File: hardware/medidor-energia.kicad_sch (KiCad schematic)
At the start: 43 parts, among them J1 Bornera 5 V, J2 Jack 3,5 mm de panel (pinza S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, J3 Jack 3,5 mm de panel (pinza S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, J4 Bornera red L/N, J5 Bornera ZMPT, J6 OLED (GND VCC SCL SDA), J7 Reserva ADC1, SW1 Pulsador de panel 12 mm NA, SW2 Pulsador de panel 12 mm NA, U1 ESP32-DevKitC V4 (38 pines), U2 Módulo ZMPT101B

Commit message: PCB de una cara para fabricar por tóner y gabinete ajustado a ella
- herramientas/generar_pcb.py: PCB de 150 × 90 mm con cobre solo abajo, ruteada con
  Freerouting (4 puentes de alambre), relleno de GND y agujeros M3; DRC sin conexiones
  pendientes ni diferencias con el esquemático
- herramientas/exportar_fabricacion.sh: PDF 1:1 para tóner, Gerber, taladros, guía de
  montaje, lista de puentes, vistas 3D y STEP
- freecad: cables hasta los pads reales (conectores.json), jacks y USB alineados con la PCB,
  tornillos M3, rótulos con tildes y vistas del medidor en Blender
- Documento: sección 7.7 (PCB y alternativa en placa perforada), materiales, cronograma,
  dificultades y anexo; diagrama de bloques con HTTP y la plataforma web
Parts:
- C1: footprint Capacitor_THT:CP_Radial_D8.0mm_P5.00mm -> Capacitor_THT:CP_Radial_D8.0mm_P3.50mm
- C10, C11: footprint Capacitor_THT:C_Disc_D5.0mm_W2.5mm_P2.50mm -> Capacitor_THT:C_Disc_D5.0mm_W2.5mm_P5.00mm
- C9: footprint Capacitor_THT:C_Disc_D7.5mm_W5.0mm_P7.50mm -> Capacitor_THT:C_Disc_D7.5mm_W5.0mm_P5.00mm
- D2, D3, D5: footprint Diode_THT:D_DO-35_SOD27_P5.08mm_Vertical_AnodeUp -> Diode_THT:D_DO-35_SOD27_P7.62mm_Horizontal
- R4: footprint Resistor_THT:R_Axial_DIN0207_L6.3mm_D2.5mm_P5.08mm_Vertical -> Resistor_THT:R_Axial_DIN0207_L6.3mm_D2.5mm_P10.16mm_Horizontal
- R8: footprint Resistor_THT:R_Axial_DIN0207_L6.3mm_D2.5mm_P7.62mm_Horizontal -> Resistor_THT:R_Axial_DIN0207_L6.3mm_D2.5mm_P10.16mm_Horizontal
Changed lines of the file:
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@@
 			)
 		)
-		(property "Footprint" "Capacitor_THT:CP_Radial_D8.0mm_P5.00mm"
+		(property "Footprint" "Capacitor_THT:CP_Radial_D8.0mm_P3.50mm"
 			(at 74.93 55.88 0)
 			(effects
@@
 			)
 		)
-		(property "Footprint" "Diode_THT:D_DO-35_SOD27_P5.08mm_Vertical_AnodeUp"
+		(property "Footprint" "Diode_THT:D_DO-35_SOD27_P7.62mm_Horizontal"
 			(at 96.52 104.14 0)
 			(effects
@@
 			)
 		)
-		(property "Footprint" "Diode_THT:D_DO-35_SOD27_P5.08mm_Vertical_AnodeUp"
+		(property "Footprint" "Diode_THT:D_DO-35_SOD27_P7.62mm_Horizontal"
 			(at 96.52 111.76 0)
 			(effects
@@
 			)
 		)
-		(property "Footprint" "Diode_THT:D_DO-35_SOD27_P5.08mm_Vertical_AnodeUp"
+		(property "Footprint" "Diode_THT:D_DO-35_SOD27_P7.62mm_Horizontal"
 			(at 96.52 157.48 0)
 			(effects
@@
 			)
 		)
-		(property "Footprint" "Resistor_THT:R_Axial_DIN0207_L6.3mm_D2.5mm_P5.08mm_Vertical"
+		(property "Footprint" "Resistor_THT:R_Axial_DIN0207_L6.3mm_D2.5mm_P10.16mm_Horizontal"
 			(at 149.86 111.76 0)
 			(effects
@@
 			)
 		)
-		(property "Footprint" "Resistor_THT:R_Axial_DIN0207_L6.3mm_D2.5mm_P7.62mm_Horizontal"
+		(property "Footprint" "Resistor_THT:R_Axial_DIN0207_L6.3mm_D2.5mm_P10.16mm_Horizontal"
 			(at 160.02 217.17 0)
 			(effects
@@
 			)
 		)
-		(property "Footprint" "Capacitor_THT:C_Disc_D7.5mm_W5.0mm_P7.50mm"
+		(property "Footprint" "Capacitor_THT:C_Disc_D7.5mm_W5.0mm_P5.00mm"
 			(at 172.72 217.17 0)
 			(effects
@@
 			)
 		)
-		(property "Footprint" "Capacitor_THT:C_Disc_D5.0mm_W2.5mm_P2.50mm"
+		(property "Footprint" "Capacitor_THT:C_Disc_D5.0mm_W2.5mm_P5.00mm"
 			(at 317.5 161.29 0)
 			(effects
@@
 			)
 		)
-		(property "Footprint" "Capacitor_THT:C_Disc_D5.0mm_W2.5mm_P2.50mm"
+		(property "Footprint" "Capacitor_THT:C_Disc_D5.0mm_W2.5mm_P5.00mm"
 			(at 317.5 189.23 0)
 			(effects

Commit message: Plataforma sobre Supabase, esquemáticos sin datos personales y redacción revisada
- plataforma: Postgres en Supabase con postgres.js (DATABASE_URL) en lugar de SQLite;
  migración en supabase/migrations con RLS activo; ingesta por lotes en una transacción;
  pnpm db:migrar y .env.ejemplo; pruebas del servicio contra un Postgres de pruebas
- Esquemáticos, PCB y figuras sin nombres ni referencias a asignaturas (revisión B)
- Redacción del documento revisada para un tono más directo y sin exagerar el avance
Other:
- company: Universidad de la Costa (CUC) — Sistemas Embebidos 1 -> (none)
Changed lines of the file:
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@@
 	(title_block
 		(title "Medidor de energía de dos canales con ESP32")
-		(date "2026-10-16")
-		(rev "C2-A")
-		(company "Universidad de la Costa (CUC) — Sistemas Embebidos 1")
-		(comment 1 "David Orozco · Jose Torres · Leo Rojas")
-		(comment 2 "Montaje en placa perforada de 2,54 mm")
+		(date "2026-10-21")
+		(rev "B")
+		(company "")
+		(comment 1 "")
+		(comment 2 "PCB de una cara (ver medidor-energia.kicad_pcb)")
 	)
 	(junction

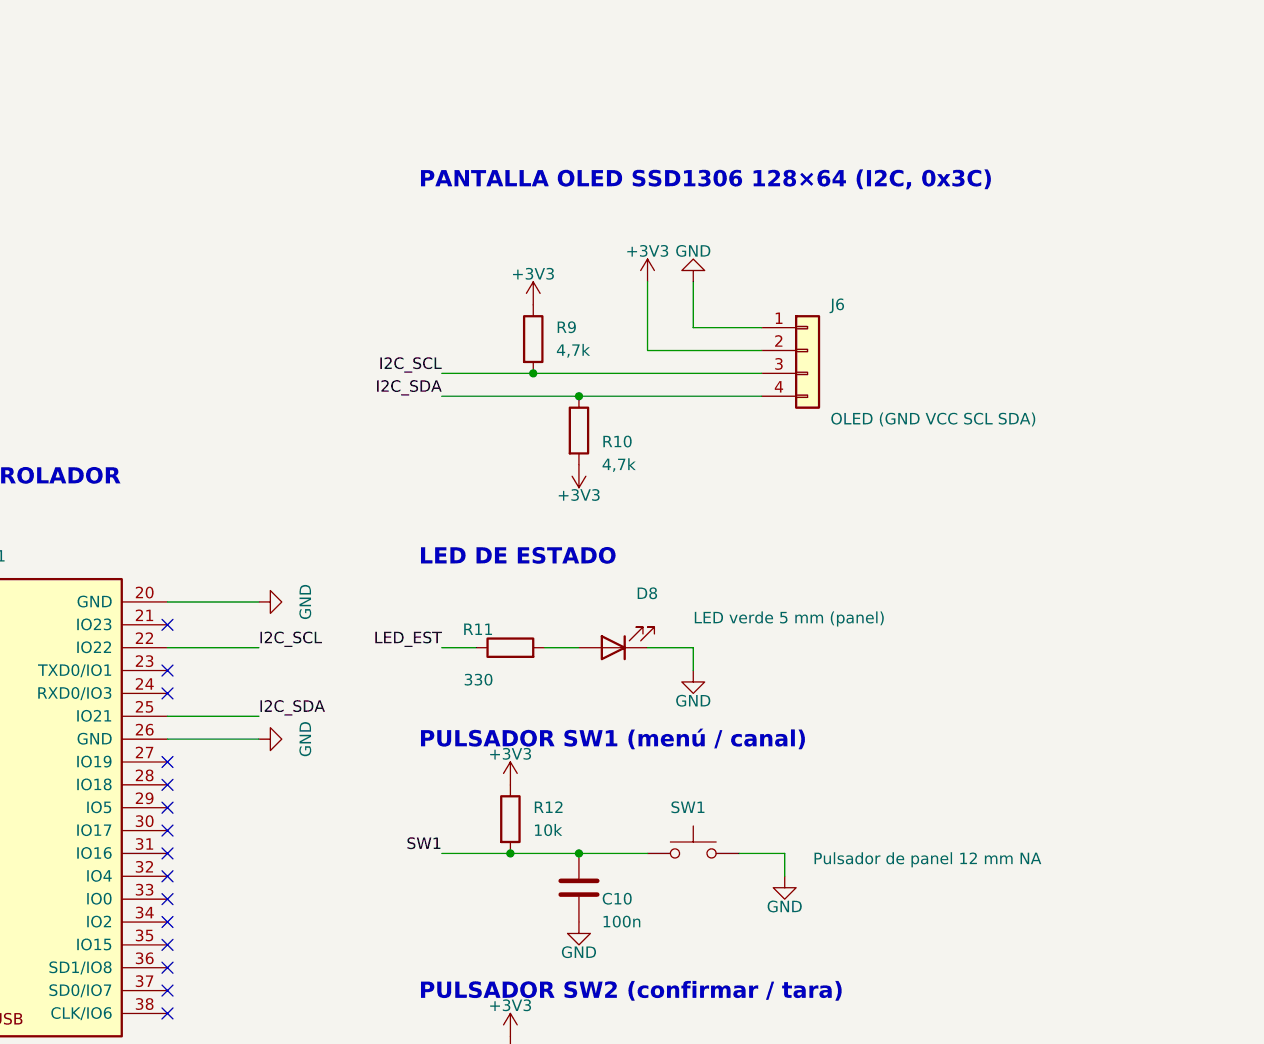
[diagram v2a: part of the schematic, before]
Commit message: LCD Waveshare de 1,9" (ST7789V2, SPI) y modo de demostración para Railway/Render
- Firmware: pantallas en lib/interfaz sobre Adafruit GFX, dibujadas por franjas; energía por hora.
- Las imágenes de las pantallas salen del mismo código compilado en el PC (make -C test pantallas).
- Esquemático: J6 de 8 pines en el orden del DevKitC; se quitan R9 y R10 (pull-up del I2C).
- PCB re-ruteada: 3 puentes, DRC sin conexiones pendientes; placa perforada verificada (25 redes).
- Tapa con ventana para la LCD, diagrama de bloques, README y diagrama de navegación.
- Plataforma: DEMO=1 corre con Postgres en memoria (PGlite) y datos del simulador; Dockerfile,
  railway.json y render.yaml.
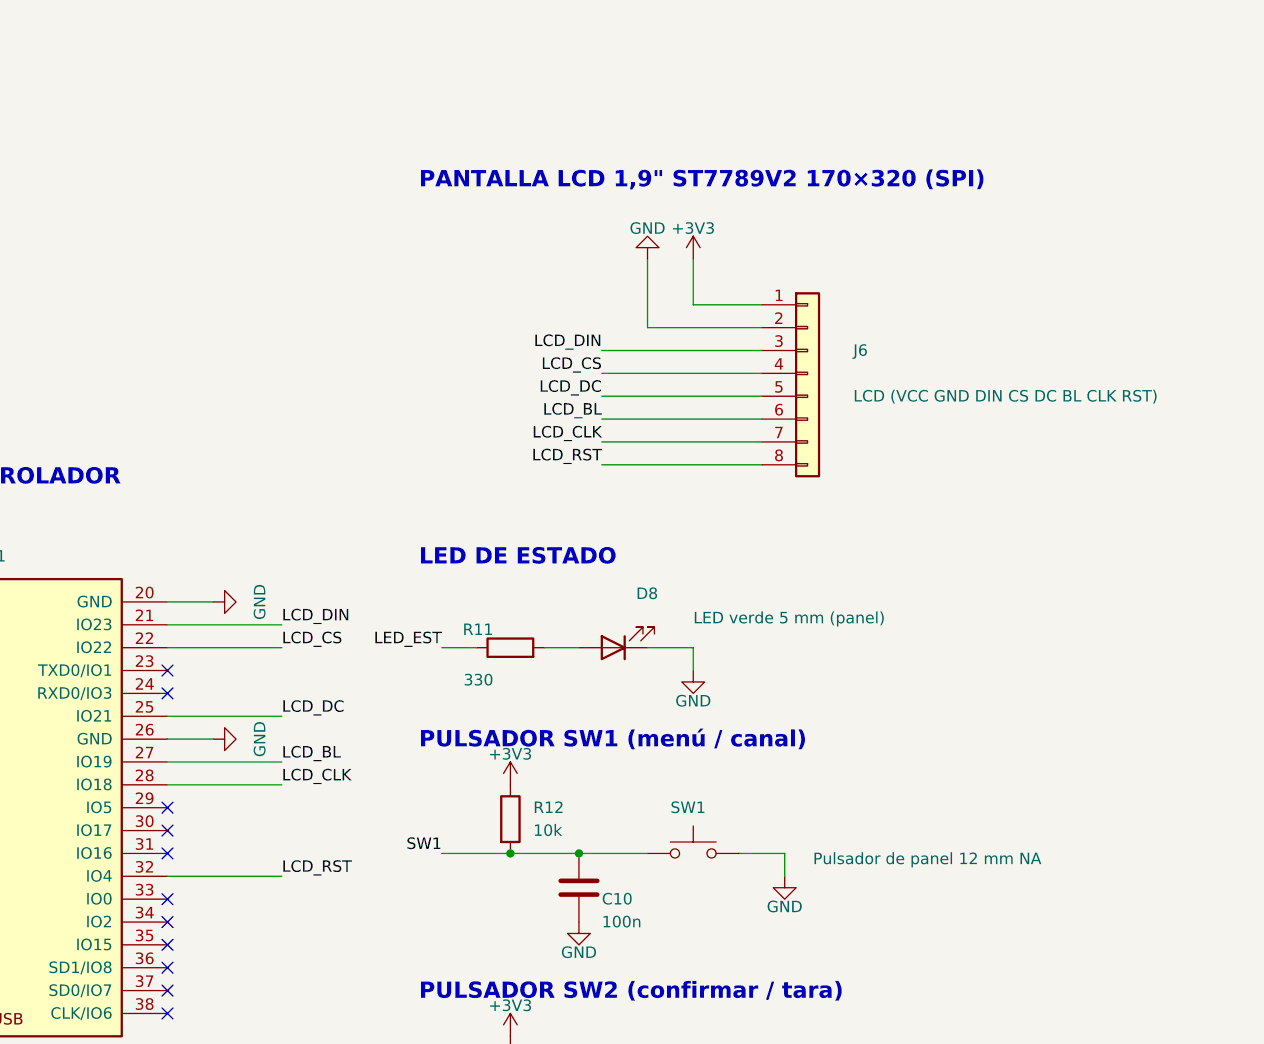
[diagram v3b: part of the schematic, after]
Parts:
- removed J7: Reserva ADC1, Connector_PinSocket_2.54mm:PinSocket_1x04_P2.54mm_Vertical, symbol Connector_Generic:Conn_01x04
- removed R13: 10k, Resistor_THT:R_Axial_DIN0207_L6.3mm_D2.5mm_P10.16mm_Horizontal, symbol Device:R
- removed SW1: Pulsador de panel 12 mm NA, Connector_PinHeader_2.54mm:PinHeader_1x02_P2.54mm_Vertical, symbol Switch:SW_Push
- added C11: 100n, Capacitor_THT:C_Disc_D5.0mm_W2.5mm_P5.00mm, symbol Device:C
- C10: renamed from D8; value LED verde 5 mm (panel) -> 100n; footprint Connector_PinHeader_2.54mm:PinHeader_1x02_P2.54mm_Vertical -> Capacitor_THT:C_Disc_D5.0mm_W2.5mm_P5.00mm; symbol Device:LED -> Device:C
- D8: renamed from R10; value 4,7k -> LED verde 5 mm (panel); footprint Resistor_THT:R_Axial_DIN0207_L6.3mm_D2.5mm_P10.16mm_Horizontal -> Connector_PinHeader_2.54mm:PinHeader_1x02_P2.54mm_Vertical; symbol Device:R -> Device:LED
- J6: value OLED (GND VCC SCL SDA) -> LCD (VCC GND DIN CS DC BL CLK RST); footprint Connector_PinSocket_2.54mm:PinSocket_1x04_P2.54mm_Vertical -> Connector_PinHeader_2.54mm:PinHeader_1x08_P2.54mm_Vertical; symbol Connector_Generic:Conn_01x04 -> Connector_Generic:Conn_01x08
- J7: renamed from C11; value 100n -> Reserva ADC1; footprint Capacitor_THT:C_Disc_D5.0mm_W2.5mm_P5.00mm -> Connector_PinSocket_2.54mm:PinSocket_1x04_P2.54mm_Vertical; symbol Device:C -> Connector_Generic:Conn_01x04
- R11: renamed from R9; value 4,7k -> 330
- R13: renamed from C10; value 100n -> 10k; footprint Capacitor_THT:C_Disc_D5.0mm_W2.5mm_P5.00mm -> Resistor_THT:R_Axial_DIN0207_L6.3mm_D2.5mm_P10.16mm_Horizontal; symbol Device:C -> Device:R
- SW1: renamed from R11; value 330 -> Pulsador de panel 12 mm NA; footprint Resistor_THT:R_Axial_DIN0207_L6.3mm_D2.5mm_P10.16mm_Horizontal -> Connector_PinHeader_2.54mm:PinHeader_1x02_P2.54mm_Vertical; symbol Device:R -> Switch:SW_Push
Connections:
- net +3V3: now also J6.1 (Pin_1), R13.1; no longer D8.2, J6.2 (Pin_2), R11.1
- net GND: now also C10.2, D8.1 (K), J6.2 (Pin_2), J7.4 (Pin_4), SW1.2, C11.2; no longer C10.1 (K), J6.1 (Pin_1), J7.2, R13.2
- net LED_EST: now also R11.1; no longer SW1.1
- net RES_IO32: now also J7.2 (Pin_2)
- net RES_IO33: now also J7.3 (Pin_3)
- net RES_IO34: now also J7.1 (Pin_1)
- net SW1: now also C10.1, SW1.1; no longer R13.1
- net SW2: now also R13.2, C11.1; no longer J7.1
- net LCD_DIN: now reaches U1.21 (IO23)
- net LCD_DIN: now also J6.3 (Pin_3)
- net LCD_BL: now reaches U1.27 (IO19)
- net LCD_BL: now also J6.6 (Pin_6)
- net LCD_CLK: now reaches U1.28 (IO18)
- net LCD_CLK: now also J6.7 (Pin_7)
- net LCD_RST: now reaches U1.32 (IO4)
- net LCD_RST: now also J6.8 (Pin_8)
- removed net I2C_SCL: J6.3 (Pin_3), R11.2, U1.22 (IO22)
- removed net I2C_SDA: D8.1, J6.4 (Pin_4), U1.25 (IO21)
- new net: D8.2 (A), R11.2
- new net LCD_CS: J6.4 (Pin_4), U1.22 (IO22)
- new net LCD_DC: J6.5 (Pin_5), U1.25 (IO21)
- no-connect marks 24 -> 20
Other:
- note added: "PANTALLA LCD 1,9" ST7789V2 170×320 (SPI)"
- note removed: "PANTALLA OLED SSD1306 128×64 (I2C, 0x3C)"
- moved on the sheet: R11

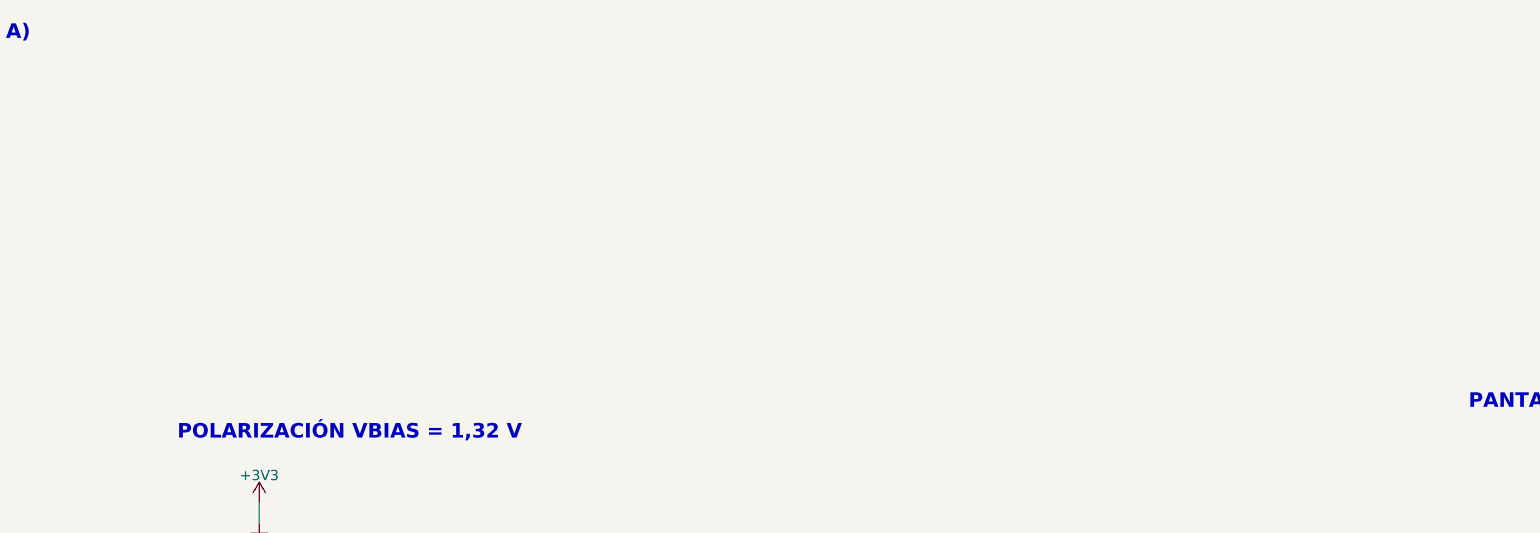
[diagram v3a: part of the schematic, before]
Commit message: Puntos de prueba TP1–TP9 y LED de alimentación en la PCB
- Lazos para la punta del osciloscopio en +5V, +3V3, VBIAS, CH1_ADC, CH2_ADC, ZMPT_OUT y V_ADC,
  y dos de GND; la serigrafía rotula la red de cada uno.
- D9 (+5 V, R14 1 kΩ) y D10 (+3,3 V, R15 470 Ω).
- PCB re-ruteada con 3 puentes; DRC sin errores ni conexiones pendientes; placa perforada con 27 redes.
- README: tabla de valores esperados en cada punto y verificación antes de energizar con los TP.
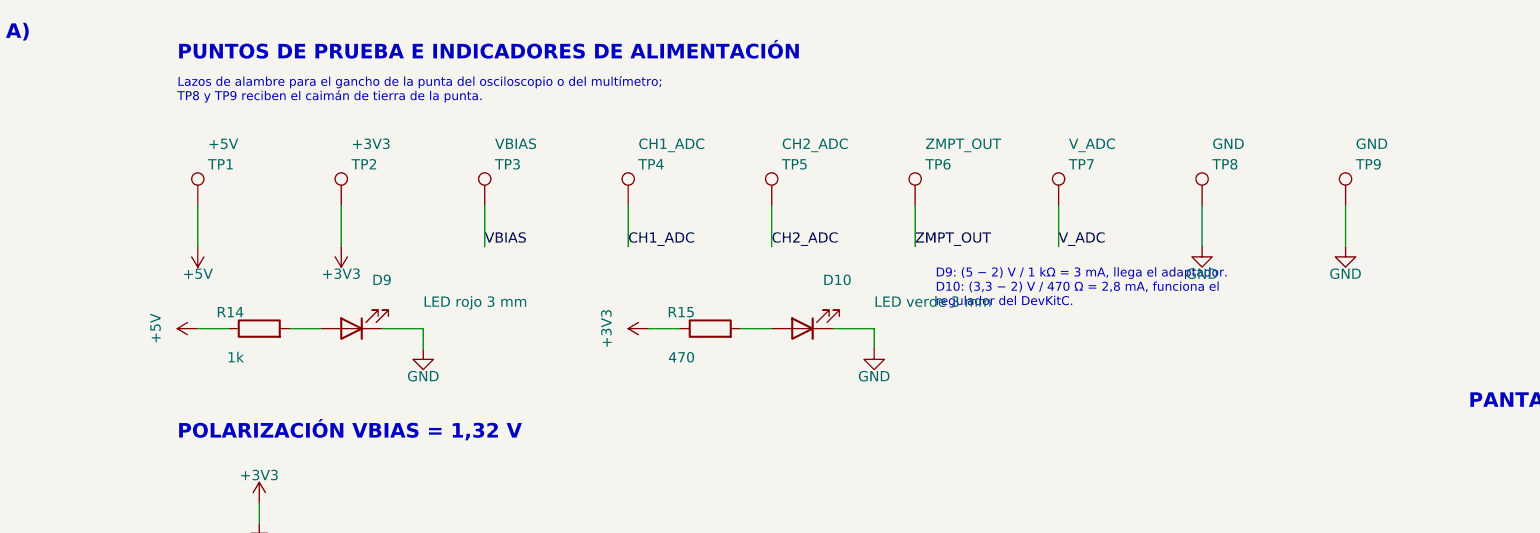
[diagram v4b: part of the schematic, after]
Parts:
- added C10, C11: 100n, Capacitor_THT:C_Disc_D5.0mm_W2.5mm_P5.00mm, symbol Device:C
- added D10: LED verde 3 mm, LED_THT:LED_D3.0mm, symbol Device:LED
- added J7: Reserva ADC1, Connector_PinSocket_2.54mm:PinSocket_1x04_P2.54mm_Vertical, symbol Connector_Generic:Conn_01x04
- added R11: 330, Resistor_THT:R_Axial_DIN0207_L6.3mm_D2.5mm_P10.16mm_Horizontal, symbol Device:R
- added R13: 10k, Resistor_THT:R_Axial_DIN0207_L6.3mm_D2.5mm_P10.16mm_Horizontal, symbol Device:R
- added R14: 1k, Resistor_THT:R_Axial_DIN0207_L6.3mm_D2.5mm_P10.16mm_Horizontal, symbol Device:R
- added R15: 470, Resistor_THT:R_Axial_DIN0207_L6.3mm_D2.5mm_P10.16mm_Horizontal, symbol Device:R
- added SW1: Pulsador de panel 12 mm NA, Connector_PinHeader_2.54mm:PinHeader_1x02_P2.54mm_Vertical, symbol Switch:SW_Push
- added TP2: +3V3, TestPoint:TestPoint_Loop_D2.50mm_Drill1.0mm, symbol Connector:TestPoint
- added TP5: CH2_ADC, TestPoint:TestPoint_Loop_D2.50mm_Drill1.0mm, symbol Connector:TestPoint
- added TP6: ZMPT_OUT, TestPoint:TestPoint_Loop_D2.50mm_Drill1.0mm, symbol Connector:TestPoint
- added TP7: V_ADC, TestPoint:TestPoint_Loop_D2.50mm_Drill1.0mm, symbol Connector:TestPoint
- D9: renamed from J7; value Reserva ADC1 -> LED rojo 3 mm; footprint Connector_PinSocket_2.54mm:PinSocket_1x04_P2.54mm_Vertical -> LED_THT:LED_D3.0mm; symbol Connector_Generic:Conn_01x04 -> Device:LED
- TP1: renamed from R11; value 330 -> +5V; footprint Resistor_THT:R_Axial_DIN0207_L6.3mm_D2.5mm_P10.16mm_Horizontal -> TestPoint:TestPoint_Loop_D2.50mm_Drill1.0mm; symbol Device:R -> Connector:TestPoint
- TP3: renamed from SW1; value Pulsador de panel 12 mm NA -> VBIAS; footprint Connector_PinHeader_2.54mm:PinHeader_1x02_P2.54mm_Vertical -> TestPoint:TestPoint_Loop_D2.50mm_Drill1.0mm; symbol Switch:SW_Push -> Connector:TestPoint
- TP4: renamed from C10; value 100n -> CH1_ADC; footprint Capacitor_THT:C_Disc_D5.0mm_W2.5mm_P5.00mm -> TestPoint:TestPoint_Loop_D2.50mm_Drill1.0mm; symbol Device:C -> Connector:TestPoint
- TP8: renamed from R13; value 10k -> GND; footprint Resistor_THT:R_Axial_DIN0207_L6.3mm_D2.5mm_P10.16mm_Horizontal -> TestPoint:TestPoint_Loop_D2.50mm_Drill1.0mm; symbol Device:R -> Connector:TestPoint
- TP9: renamed from C11; value 100n -> GND; footprint Capacitor_THT:C_Disc_D5.0mm_W2.5mm_P5.00mm -> TestPoint:TestPoint_Loop_D2.50mm_Drill1.0mm; symbol Device:C -> Connector:TestPoint
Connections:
- net +3V3: now also R13.1, R15.1, TP2.1; no longer TP8.1
- net +5V: now also TP1.1, R14.1
- net CH1_ADC: now also TP4.1
- net CH2_ADC: now also TP5.1
- net GND: now also D9.1 (K), TP8.1, TP9.1, C10.2, C11.2, D10.1 (K), J7.4 (Pin_4), SW1.2; no longer D9.4 (Pin_4), TP3.2, TP4.2, TP9.2
- net LED_EST: now also R11.1; no longer TP1.1
- net RES_IO32: now also J7.2 (Pin_2); no longer D9.2 (Pin_2)
- net RES_IO33: now also J7.3 (Pin_3); no longer D9.3 (Pin_3)
- net RES_IO34: now also J7.1 (Pin_1); no longer D9.1 (Pin_1)
- net SW1: now also C10.1, SW1.1; no longer TP3.1, TP4.1
- net SW2: now also C11.1, R13.2; no longer TP8.2, TP9.1
- net VBIAS: now also TP3.1
- net V_ADC: now also TP7.1
- net ZMPT_OUT: now also TP6.1
- net at D8.2 (A): now also R11.2; no longer TP1.2
- new net: D10.2 (A), R15.2
- new net: D9.2 (A), R14.2
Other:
- note added: "D9: (5 − 2) V / 1 kΩ = 3 mA, llega el adaptador. D10: (3,3 − 2) V / 470 Ω = 2,8 mA, funciona el regulador del DevKitC."
- note added: "Lazos de alambre para el gancho de la punta del osciloscopio o del multímetro; TP8 y TP9 reciben el caimán de tierra de la punta."
- note added: "PUNTOS DE PRUEBA E INDICADORES DE ALIMENTACIÓN"
